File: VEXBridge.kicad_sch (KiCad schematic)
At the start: 28 parts, among them J1 4P4C, J3 Conn_01x05_Pin, U1 LM2596S-5, U2 MAX481E, U5 SN74LVC2G14DBV

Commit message: VEXBridge v2 (WIP)
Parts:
- removed D3: LED, LED_SMD:LED_0603_1608Metric, symbol Device:LED
- removed D4: ESDA5V3L, Package_TO_SOT_SMD:SOT-23-3, symbol Power_Protection:ESDA5V3L
- removed J3: Conn_01x05_Pin, Connector_PinHeader_2.54mm:PinHeader_1x05_P2.54mm_Vertical, symbol Connector:Conn_01x05_Pin
- removed U1: LM2596S-5, Package_TO_SOT_SMD:TO-263-5_TabPin3, symbol Regulator_Switching:LM2596S-5
- removed U2: MAX481E, Package_SO:SOIC-8_3.9x4.9mm_P1.27mm, symbol Interface_UART:MAX481E
- removed U5: SN74LVC2G14DBV, Package_TO_SOT_SMD:SOT-23-6, symbol 74xGxx:SN74LVC2G14DBV
- added C6: 10uF, Capacitor_SMD:C_0201_0603Metric, symbol Device:C
- added C7: 22uF, Capacitor_SMD:C_1206_3216Metric, symbol Device:C
- added C8: 1uF, Capacitor_SMD:C_0201_0603Metric, symbol Device:C
- added D3: D, Diode_SMD:D_0201_0603Metric, symbol Device:D
- added F1: 1A, Fuse:Fuse_2010_5025Metric, symbol Device:Polyfuse
- added J10, J4, J5, J9: QWIIC Connector, Connector_JST:JST_SH_SM04B-SRSS-TB_1x04-1MP_P1.00mm_Horizontal, symbol Connector_Generic_MountingPin:Conn_01x04_MountingPin
- added J2, J3, J6, J7: Conn_01x04, Connector_Molex:Molex_PicoBlade_53047-0410_1x04_P1.25mm_Vertical, symbol Connector_Generic:Conn_01x04
- added J8: USB_C_Receptacle_USB2.0_14P, Connector_USB:USB_C_Plug_Molex_105444, symbol Connector:USB_C_Receptacle_USB2.0_14P
- added R10: 10k, Resistor_SMD:R_0805_2012Metric, symbol Device:R
- added R11, R13, R14: 5.1k, Resistor_SMD:R_0805_2012Metric, symbol Device:R
- added U2: ESP32-S3-MINI-1U, RF_Module:ESP32-S2-MINI-1U, symbol RF_Module:ESP32-S3-MINI-1U
- added U3: LSM9DS1, Package_LGA:LGA-24L_3x3.5mm_P0.43mm, symbol Sensor_Motion:LSM9DS1
- added U4: AMS1117-3.3, Package_TO_SOT_SMD:SOT-223-3_TabPin2, symbol Regulator_Linear:AMS1117-3.3
- added U5: LM2595S-5, Package_TO_SOT_SMD:TO-263-5_TabPin3, symbol Regulator_Switching:LM2595S-5
- C1: value 100uF -> 220uF; footprint Capacitor_SMD:CP_Elec_6.3x7.7 -> Capacitor_SMD:C_1210_3225Metric
- C2: value 220uF -> 100uF; footprint Capacitor_SMD:CP_Elec_6.3x7.7 -> Capacitor_SMD:C_1206_3216Metric
- C3, C4: value 0.1uF -> 1uF; footprint Capacitor_SMD:C_0402_1005Metric -> Capacitor_SMD:C_0201_0603Metric
- D1: value LED -> RED
- D2: value LED -> GREEN
- L1: value 47uH -> 68uH; footprint Inductor_SMD:L_Coilcraft_LPS4018 -> Inductor_SMD:L_SXN_SMDRI127
- R1: value 100 -> 5.1k
- R2: value 120 -> 10k; footprint Resistor_SMD:R_1206_3216Metric -> Resistor_SMD:R_0805_2012Metric
- R3, R4: value 100 -> 10k
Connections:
- net RTS is gone; now on net +3.3V: R8.1
- net TXD is gone; now on net SDA: R7.2
- net +12V: now also F1.2, U5.2 (VIN); no longer J1.4
- net +5V: now also C6.1, D3.1 (K), J2.1 (Pin_1), J3.1 (Pin_1), J6.1 (Pin_1), J7.1 (Pin_1), U4.3 (VI), U5.4 (FB); no longer C3.1, C4.1, R1.1, R6.1, R7.1, R9.1
- net GND: now also C6.2, C7.2, C8.2, J10.1 (Pin_1), J10.MP (MountPin), J2.4 (Pin_4), J3.4 (Pin_4), J4.1 (Pin_1), J4.MP (MountPin), J5.1 (Pin_1), J5.MP (MountPin), J6.4 (Pin_4), J7.4 (Pin_4), J8.A1 (GND), J8.A12 (GND), J8.B1 (GND), J8.B12 (GND), J8.S1 (SHIELD), J9.1 (Pin_1), J9.MP (MountPin), R13.2, R14.2, U2.1 (GND), U2.2 (GND), U2.42 (GND), U2.43 (GND), U2.46 (GND), U2.47 (GND), U2.48 (GND), U2.49 (GND), U2.50 (GND), U2.51 (GND), U2.52 (GND), U2.53 (GND), U2.54 (GND), U2.55 (GND), U2.56 (GND), U2.57 (GND), U2.58 (GND), U2.59 (GND), U2.60 (GND), U2.61 (GND), U2.62 (GND), U2.63 (GND), U2.64 (GND), U2.65 (GND), U3.19 (GND), U3.20 (GND), U4.1 (GND), U5.3 (GND), U5.5 (ON/~{OFF}); no longer R5.2, R8.2
- net +3.3V: now reaches R4.1
- net +3.3V: now also C3.1, C4.1, R1.2, R2.1, R3.1, R5.1, R6.1, R7.1, R9.1, C7.1, J10.2 (Pin_2), J4.2 (Pin_2), J5.2 (Pin_2), J9.2 (Pin_2), R10.1, U2.3 (3V3), U3.22 (VDD), U3.23 (VDD), U4.2 (VO)
- net SDA: now reaches R4.2
- net SDA: now also R3.2, R6.2, J10.3 (Pin_3), J4.3 (Pin_3), J5.3 (Pin_3), J9.3 (Pin_3), U2.4 (IO0), U3.4 (SDA/SDI/SDO)
- net at D9.1 (K), L1.1: now also U5.1 (OUT)
- net at D1.2 (A): now also R1.1; no longer R1.2
- net at D2.2 (A): now also R11.1; no longer R3.2
- removed net A: J1.1, R2.2, R6.2
- removed net B: J1.2, R2.1, R5.1
- net RXD renamed SCL
- net SCL: now also R5.2, R8.2, J10.4 (Pin_4), J4.4 (Pin_4), J5.4 (Pin_4), J9.4 (Pin_4), R10.2, U2.5 (IO1), U3.2 (SCL/SPC)
- new net: F1.1, J1.4
- new net: C8.1, R2.2, U2.45 (EN)
- new net: U3.1 (VDDIO), U3.3 (VDDIO)
- new net: J8.B5 (CC2), R13.1
- new net: J8.A5 (CC1), R14.1
- new net: D3.2 (A), J8.A4 (VBUS), J8.A9 (VBUS), J8.B4 (VBUS), J8.B9 (VBUS)
- new net ENC_A1: J3.2 (Pin_2), U2.8 (IO4)
- new net ENC_A2: J6.2 (Pin_2), U2.10 (IO6)
- new net ENC_A3: J2.2 (Pin_2), U2.12 (IO8)
- new net ENC_A4: J7.2 (Pin_2), U2.14 (IO10)
- new net ENC_B1: J3.3 (Pin_3), U2.9 (IO5)
- new net ENC_B2: J6.3 (Pin_3), U2.11 (IO7)
- new net ENC_B3: J2.3 (Pin_3), U2.13 (IO9)
- new net ENC_B4: J7.3 (Pin_3), U2.15 (IO11)
- new net LED_IO: R11.2, U2.25 (IO21)
- new net USB_D+: J8.A6 (D+), J8.B6 (D+), U2.24 (IO20)
- new net USB_D-: J8.A7 (D-), J8.B7 (D-), U2.23 (IO19)
- no-connect marks 0 -> 45
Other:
- note added: "12V to 5V Step-down"
- note added: "5V to 3.3V Step-down"
- note added: "Diagnostic LEDs"
- note added: "ESP32 Pinout"
- note added: "Encoder Connectors"
- note added: "Grounded Mounting Holes"
- note added: "Integrated IMU"
- note added: "QWIIC I2C Connectors"
- note added: "USB-C Interface"
- note added: "VEX V5 Interface"
- note removed: "12V to 5V Step-down (Max 3A)"
- note removed: "INPUT"
- note removed: "LEDs"
- note removed: "Output"
- note removed: "POWER"
- note removed: "RS-485 Tranceiver"
- note removed: "RX/TX"
- moved on the sheet: C1, C2, D1, D9, H1, H2, H3, H4, J1, L1, R1

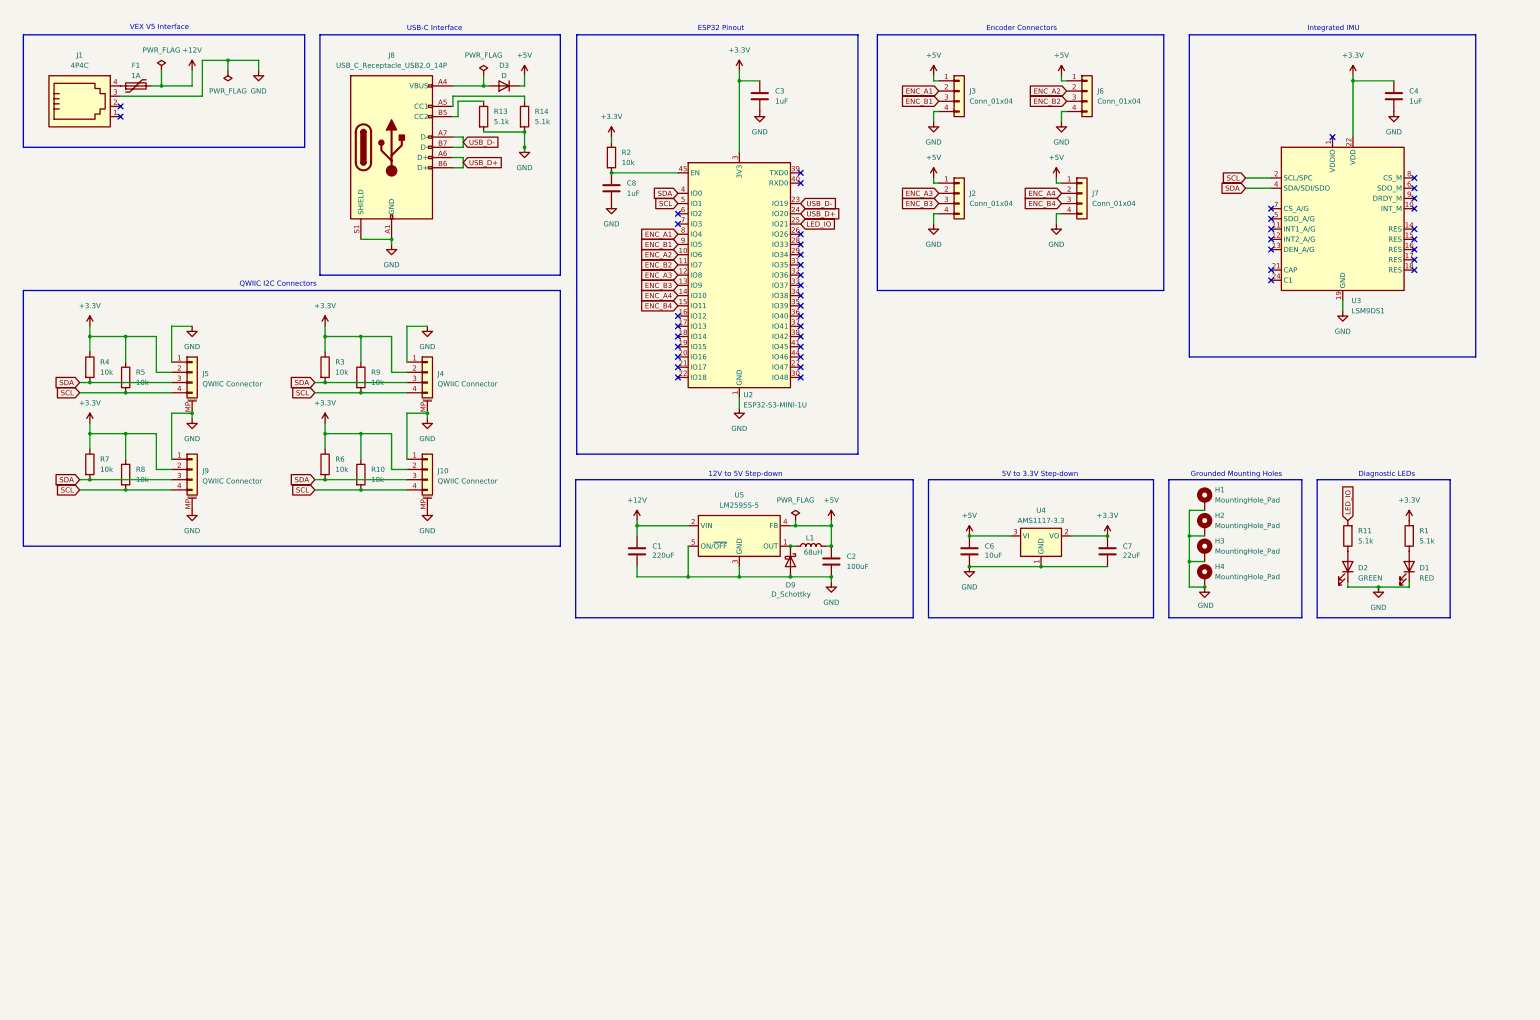
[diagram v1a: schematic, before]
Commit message: Added a 8 bit multiplexer
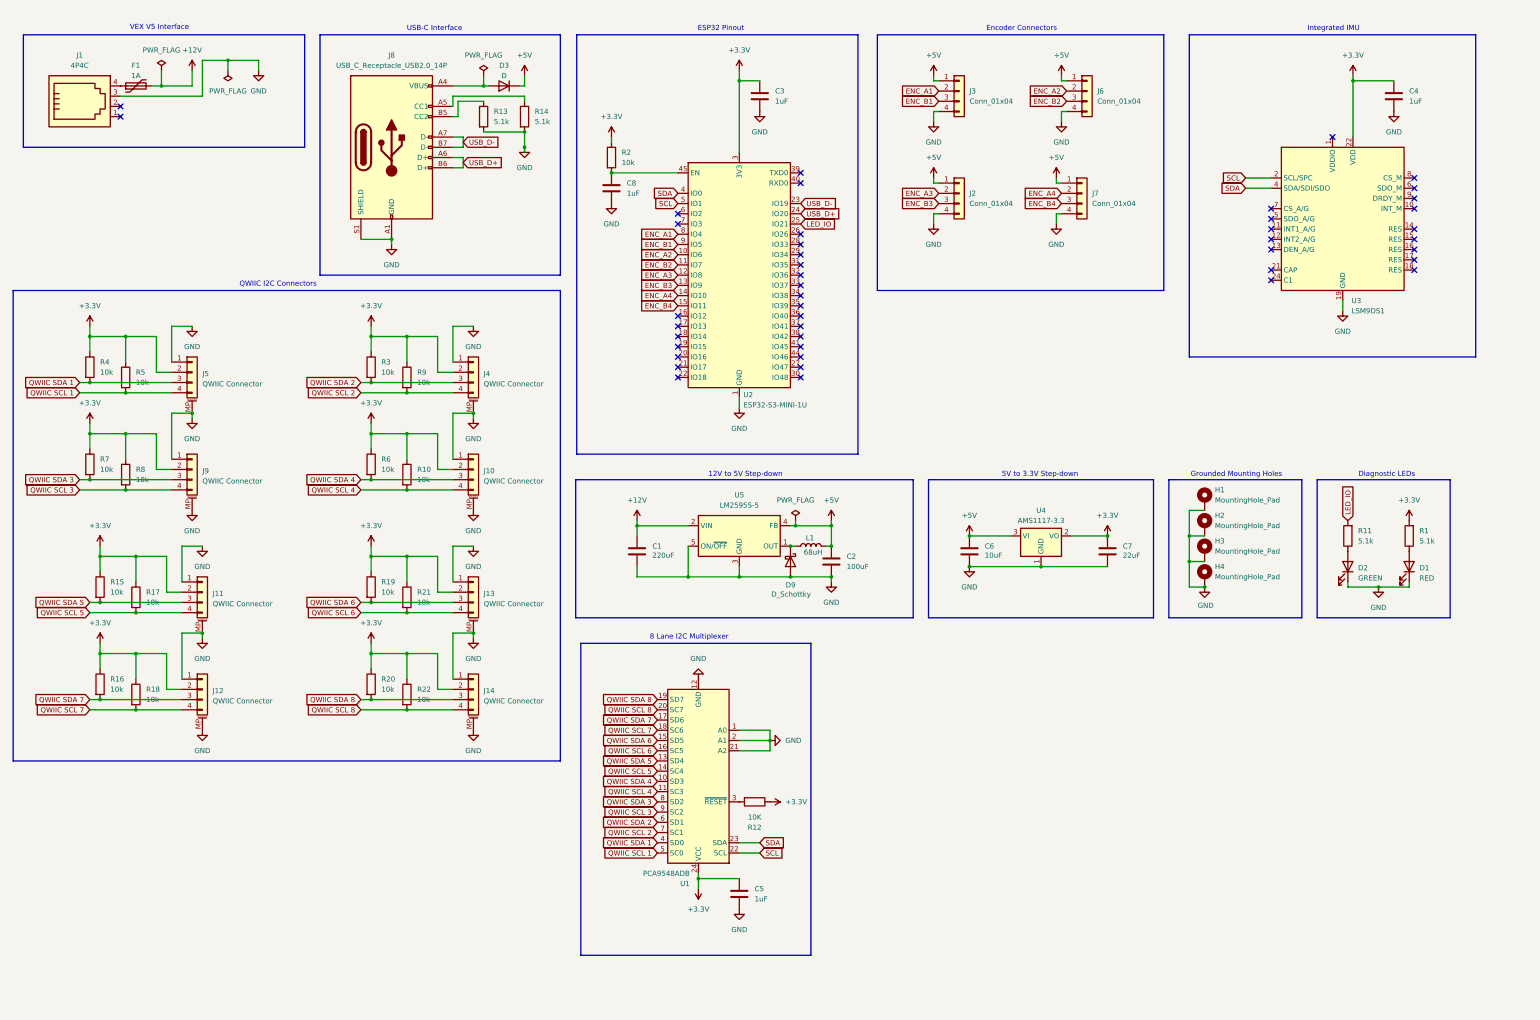
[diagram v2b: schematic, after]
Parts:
- added C5: 1uF, Capacitor_SMD:C_0201_0603Metric, symbol Device:C
- added J11, J12, J13, J14: QWIIC Connector, Connector_JST:JST_SH_SM04B-SRSS-TB_1x04-1MP_P1.00mm_Horizontal, symbol Connector_Generic_MountingPin:Conn_01x04_MountingPin
- added R12: 10K, symbol Device:R
- added R15, R16, R17, R18, R19, R20, R21, R22: 10k, Resistor_SMD:R_0805_2012Metric, symbol Device:R
- added U1: PCA9548ADB, Package_SO:SSOP-24_5.3x8.2mm_P0.65mm, symbol Interface_Expansion:PCA9548ADB
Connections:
- net +3.3V: now also C5.1, J11.2 (Pin_2), J12.2 (Pin_2), J13.2 (Pin_2), J14.2 (Pin_2), R12.1, R15.1, R16.1, R17.1, R18.1, R19.1, R20.1, R21.1, R22.1, U1.24 (VCC)
- net GND: now also C5.2, J11.1 (Pin_1), J11.MP (MountPin), J12.1 (Pin_1), J12.MP (MountPin), J13.1 (Pin_1), J13.MP (MountPin), J14.1 (Pin_1), J14.MP (MountPin), U1.1 (A0), U1.12 (GND), U1.2 (A1), U1.21 (A2)
- net SCL: now also U1.22 (SCL); no longer J10.4 (Pin_4), J4.4 (Pin_4), J5.4 (Pin_4), J9.4 (Pin_4), R10.2, R5.2, R8.2, R9.2
- net SDA: now also U1.23 (SDA); no longer J10.3 (Pin_3), J4.3 (Pin_3), J5.3 (Pin_3), J9.3 (Pin_3), R3.2, R4.2, R6.2, R7.2
- new net: R12.2, U1.3 (~{RESET})
- new net QWIIC SCL 1: J5.4 (Pin_4), R5.2, U1.5 (SC0)
- new net QWIIC SCL 2: J4.4 (Pin_4), R9.2, U1.7 (SC1)
- new net QWIIC SCL 3: J9.4 (Pin_4), R8.2, U1.9 (SC2)
- new net QWIIC SCL 4: J10.4 (Pin_4), R10.2, U1.11 (SC3)
- new net QWIIC SCL 5: J11.4 (Pin_4), R17.2, U1.14 (SC4)
- new net QWIIC SCL 6: J13.4 (Pin_4), R21.2, U1.16 (SC5)
- new net QWIIC SCL 7: J12.4 (Pin_4), R18.2, U1.18 (SC6)
- new net QWIIC SCL 8: J14.4 (Pin_4), R22.2, U1.20 (SC7)
- new net QWIIC SDA 1: J5.3 (Pin_3), R4.2, U1.4 (SD0)
- new net QWIIC SDA 2: J4.3 (Pin_3), R3.2, U1.6 (SD1)
- new net QWIIC SDA 3: J9.3 (Pin_3), R7.2, U1.8 (SD2)
- new net QWIIC SDA 4: J10.3 (Pin_3), R6.2, U1.10 (SD3)
- new net QWIIC SDA 5: J11.3 (Pin_3), R15.2, U1.13 (SD4)
- new net QWIIC SDA 6: J13.3 (Pin_3), R19.2, U1.15 (SD5)
- new net QWIIC SDA 7: J12.3 (Pin_3), R16.2, U1.17 (SD6)
- new net QWIIC SDA 8: J14.3 (Pin_3), R20.2, U1.19 (SD7)
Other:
- note added: "8 Lane I2C Multiplexer"
- moved on the sheet: J10, J4, R10, R3, R6, R9

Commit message: Update VEXBridge.kicad_sch
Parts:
- removed C8: 1uF, Capacitor_SMD:C_0201_0603Metric, symbol Device:C
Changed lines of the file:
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@@
 	)
 	(junction
-		(at 165.1 54.61)
-		(diameter 0)
-		(color 0 0 0 0)
-	)
-	(junction
 		(at 130.81 168.91)
 		(diameter 0)
@@
 	)
 	(symbol
-		(lib_id "Device:C")
-		(at 165.1 58.42 0)
-		(unit 1)
-		(exclude_from_sim no)
-		(in_bom yes)
-		(on_board yes)
-		(dnp no)
-		(fields_autoplaced yes)
-		(property "Reference" "C8"
-			(at 168.91 57.1499 0)
-			(effects
-				(font
-					(size 1.27 1.27)
-				)
-				(justify left)
-			)
-		)
-		(property "Value" "1uF"
-			(at 168.91 59.6899 0)
-			(effects
-				(font
-					(size 1.27 1.27)
-				)
-				(justify left)
-			)
-		)
-		(property "Footprint" "Capacitor_SMD:C_0201_0603Metric"
-			(at 166.0652 62.23 0)
-			(effects
-				(font
-					(size 1.27 1.27)
-				)
-				(hide yes)
-			)
-		)
-		(property "Datasheet" "~"
-			(at 165.1 58.42 0)
-			(effects
-				(font
-					(size 1.27 1.27)
-				)
-				(hide yes)
-			)
-		)
-		(property "Description" "Unpolarized capacitor"
-			(at 165.1 58.42 0)
-			(effects
-				(font
-					(size 1.27 1.27)
-				)
-				(hide yes)
-			)
-		)
-		(pin "2"
-		)
-		(pin "1"
-		)
-		(instances
-			(project "VEXBridge"
-				(path "/75715a9c-a502-40d6-b270-e5c0bc6847fe"
-					(reference "C8")
-					(unit 1)
-				)
-			)
-		)
-	)
-	(symbol
 		(lib_id "Device:L")
 		(at 214.63 147.32 90)
@@
 					(unit 1)
 				)
-			)
-		)
-	)
-	(symbol
-		(lib_id "power:GND")
-		(at 165.1 62.23 0)
-		(unit 1)
-		(exclude_from_sim no)
-		(in_bom yes)
-		(on_board yes)
-		(dnp no)
-		(fields_autoplaced yes)
-		(property "Reference" "#PWR09"
-			(at 165.1 68.58 0)
-			(effects
-				(font
-					(size 1.27 1.27)
-				)
-				(hide yes)
-			)
-		)
-		(property "Value" "GND"
-			(at 165.1 67.31 0)
-			(effects
-				(font
-					(size 1.27 1.27)
-				)
-			)
-		)
-		(property "Footprint" ""
-			(at 165.1 62.23 0)
-			(effects
-				(font
-					(size 1.27 1.27)
-				)
-				(hide yes)
-			)
-		)
-		(property "Datasheet" ""
-			(at 165.1 62.23 0)
-			(effects
-				(font
-					(size 1.27 1.27)
-				)
-				(hide yes)
-			)
-		)
-		(property "Description" "Power symbol creates a global label with name \"GND\" , ground"
-			(at 165.1 62.23 0)
-			(effects
-				(font
-					(size 1.27 1.27)
-				)
-				(hide yes)
-			)
-		)
-		(pin "1"
-		)
-		(instances
-			(project "VEXBridge"
-				(path "/75715a9c-a502-40d6-b270-e5c0bc6847fe"
-					(reference "#PWR09")
-					(unit 1)
-				)
